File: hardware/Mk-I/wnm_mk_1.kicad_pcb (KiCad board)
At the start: 2 copper layers, 96.5 x 67.1 mm, 126 parts, among them CON1 USB-MICRO-B, SW1 SW_PUSH, SW10 SW_PUSH, SW11 SW_PUSH, SW12 SW_PUSH, SW13 SW_PUSH, SW14 SW_PUSH, SW15 SW_PUSH, SW16 SW_PUSH, SW18 SW_PUSH, SW19 SW_PUSH, SW2 SW_PUSH, SW20 SW_PUSH, SW21 SW_PUSH, SW22 SW_PUSH, SW3 SW_PUSH, SW4 SW_PUSH, SW5 SW_PUSH, SW6 SW_PUSH, SW7 SW_PUSH, SW8 SW_PUSH, SW9 SW_PUSH, U1 AP7313-18-SR-G-7, U10 STM32_SWD_Connector, U2 MCP73831, U3 BD33IA5, U4 STM32F407VG, U5 SGTL5000, U6 encoder_and_switch, U7 encoder_and_switch, U8 MOLEX_microSD_47219-2001, U9 SSD1306, X1 CRYSTAL

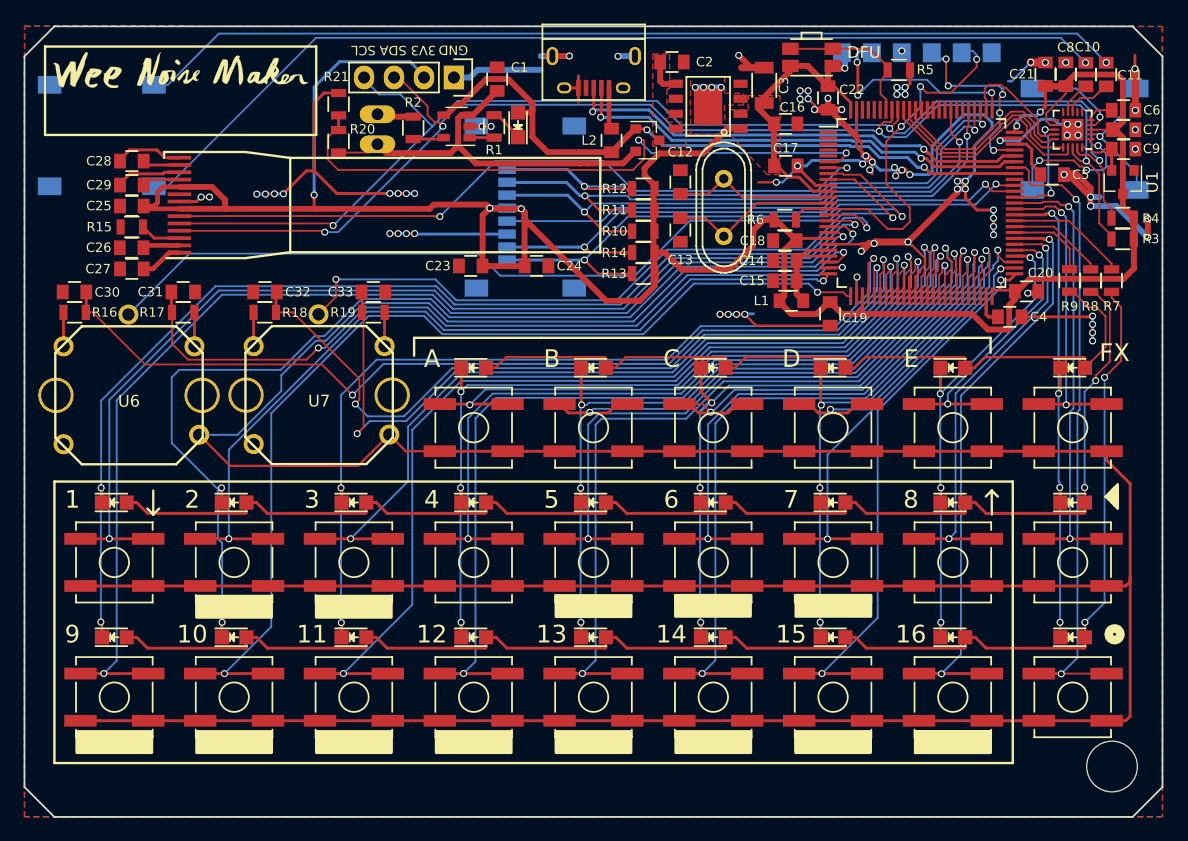
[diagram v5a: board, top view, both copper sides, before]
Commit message: HW: A couple of improvements in layout and ground
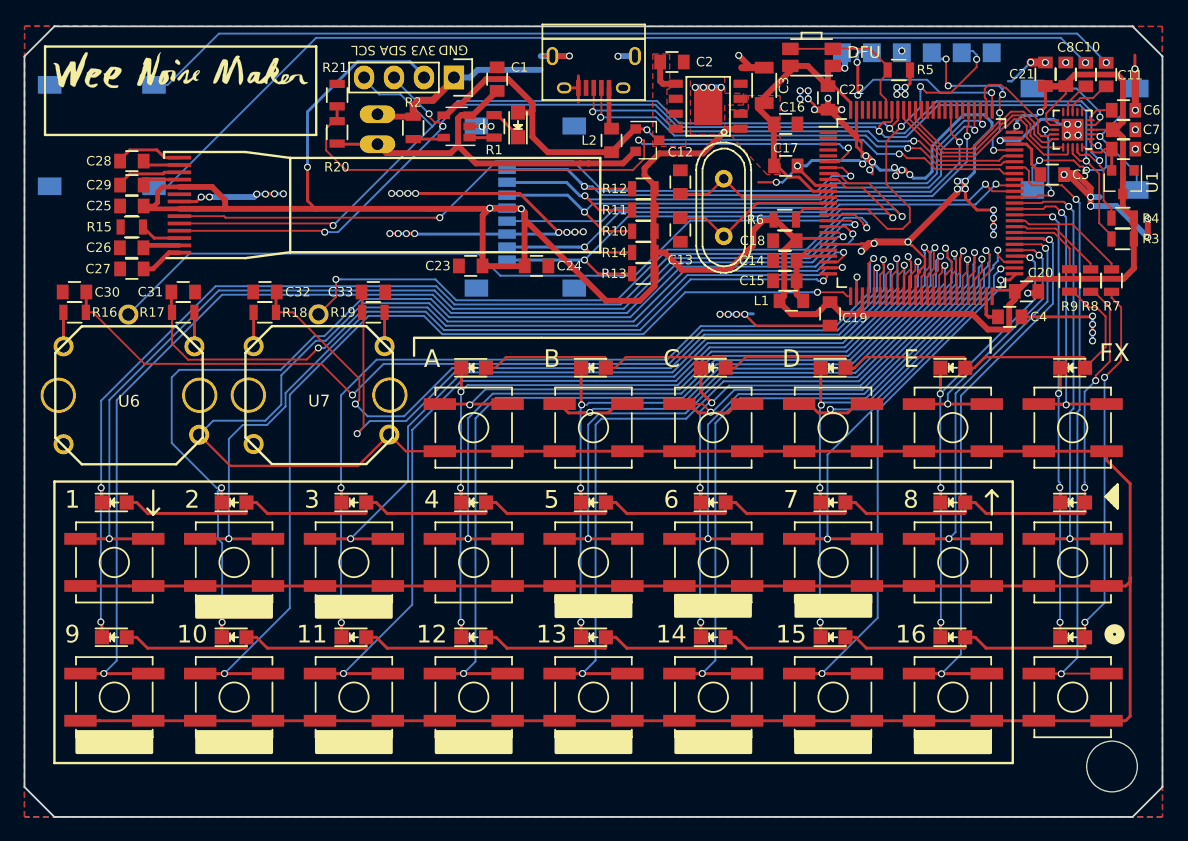
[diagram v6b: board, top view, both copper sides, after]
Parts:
- moved R21 0.78 mm to (106.5, 83.6)
- moved R20 0.77 mm to (106.5, 86.7)
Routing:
- net GND: track 211.1 -> 222.1 mm, vias 84 -> 88
- net B2: track 74.3 -> 75.5 mm
- net VBAT: track 33.9 -> 34.8 mm
- net Screen_NReset: track 62.0 -> 62.7 mm
- net WAKEUP: track 347.6 -> 348.3 mm
- net 3V3: track 245.3 -> 244.6 mm
- net B10: track 87.0 -> 86.3 mm
- net VBAT_SENSE: track 54.3 -> 54.8 mm
- net Audio_SDA: track 107.2 -> 107.0 mm, vias 4 -> 5

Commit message: HW: Enlarge screen footprint
To give room for more models.
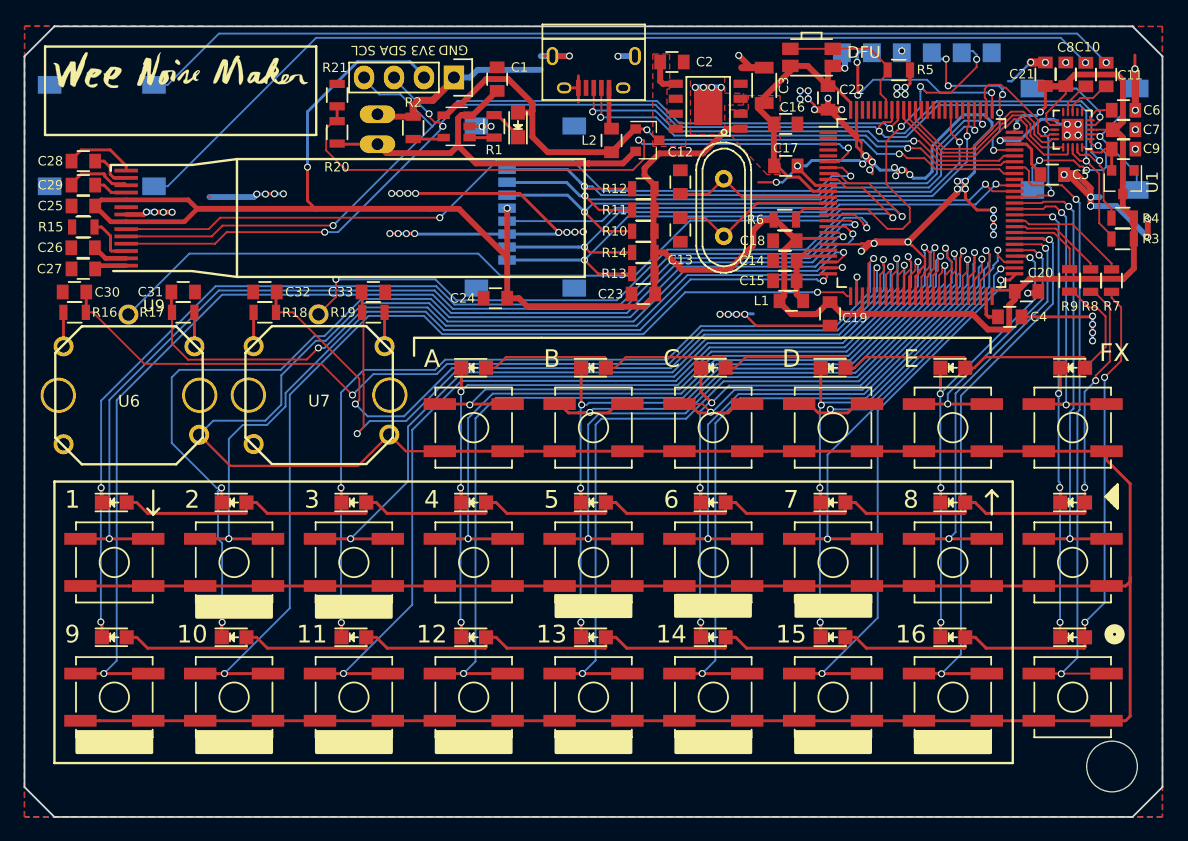
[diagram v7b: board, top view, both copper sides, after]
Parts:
- moved C23 14.8 mm to (132.5, 100.4)
- moved U9 4.65 mm to (87.4, 98.4)
- moved C24 4.44 mm to (120.0, 100.8), turned to 180 degrees
- moved C25 4.11 mm to (85.0, 93.0)
- moved C27 4.11 mm to (85.0, 98.3)
- moved C28 4.11 mm to (85.0, 89.2)
- moved C29 4.11 mm to (85.0, 91.2)
- moved R15 4.11 mm to (85.0, 94.7)
- moved C26 4.11 mm to (85.0, 96.5)
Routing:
- net Audio_SDA: track 107.0 -> 111.9 mm
- net Screen_NReset: track 62.7 -> 67.6 mm
- net Audio_SCL: track 107.2 -> 112.1 mm
- net 3V3: track 244.6 -> 240.4 mm, vias 6 -> 5
- net GND: track 222.1 -> 223.4 mm, vias 88 -> 90
- net Net-(C28-Pad2): track 3.17 -> 4.03 mm
- net Net-(C27-Pad1): track 3.60 -> 2.75 mm
- net Net-(R15-Pad1): track 3.47 -> 4.23 mm
- net Net-(C28-Pad1): track 6.61 -> 6.07 mm

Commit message: HW: Mk-I rev-C
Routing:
- net (no net): track 0.00 -> 6.39 mm, vias 0 -> 4
- net GND: track 223.4 -> 217.0 mm, vias 90 -> 86
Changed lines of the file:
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@@
-(kicad_pcb (version 4) (host pcbnew 4.0.5-e0-6337~52~ubuntu16.10.1)
+(kicad_pcb (version 4) (host pcbnew 4.0.6-e0-6349~52~ubuntu16.10.1)
   (general
     (links 345)
     (no_connects 0)
-    (area 79.933819 77.646179 176.605001 144.855001)
+    (area 66.563202 67.150001 181.907143 146.975)
     (thickness 1.6)
     (drawings 88)
@@
   )
   (setup
-    (last_trace_width 0.5)
+    (last_trace_width 0.25)
     (user_trace_width 0.16)
     (user_trace_width 0.2)
@@
       (drillshape 0)
       (scaleselection 1)
-      (outputdirectory Rev_B/gerber/))
+      (outputdirectory Rev_C/gerber/))
   )
   (net 0 "")
@@
     (effects (font (size 1.5 1.5) (thickness 0.3)))
   )
+  (segment (start 95.7 92.2) (end 99.4644 92.2) (width 0.5) (layer B.Cu) (net 0))
+  (segment (start 99.4644 92.2) (end 99.7116 91.9528) (width 0.5) (layer B.Cu) (net 0))
+  (segment (start 100.4482 91.9528) (end 99.7116 91.9528) (width 0.25) (layer B.Cu) (net 0))
+  (via (at 99.7116 91.9528) (size 0.6) (drill 0.4) (layers F.Cu B.Cu) (net 0))
+  (segment (start 101.2102 91.9274) (end 100.4736 91.9274) (width 0.25) (layer F.Cu) (net 0))
+  (segment (start 100.4736 91.9274) (end 100.4482 91.9528) (width 0.25) (layer F.Cu) (net 0))
+  (via (at 100.4482 91.9528) (size 0.6) (drill 0.4) (layers F.Cu B.Cu) (net 0))
+  (segment (start 101.9722 91.9274) (end 101.2102 91.9274) (width 0.25) (layer B.Cu) (net 0))
+  (via (at 101.2102 91.9274) (size 0.6) (drill 0.4) (layers F.Cu B.Cu) (net 0))
+  (via (at 101.9722 91.9274) (size 0.6) (drill 0.4) (layers F.Cu B.Cu) (net 0))
+  (segment (start 95.698 92.202) (end 95.7 92.2) (width 0.25) (layer F.Cu) (net 0))
   (segment (start 130.561477 101.315123) (end 134.854074 97.022526) (width 0.16) (layer B.Cu) (net 1))
   (segment (start 134.854074 97.022526) (end 146.470931 97.022525) (width 0.16) (layer B.Cu) (net 1))
@@
   (segment (start 125.1792 95.3436) (end 125.3236 95.1992) (width 0.25) (layer B.Cu) (net 31))
   (via (at 125.3236 95.1992) (size 0.6) (drill 0.4) (layers F.Cu B.Cu) (net 31))
-  (segment (start 95.7 92.2) (end 99.4644 92.2) (width 0.5) (layer B.Cu) (net 31))
-  (segment (start 99.4644 92.2) (end 99.7116 91.9528) (width 0.5) (layer B.Cu) (net 31))
-  (segment (start 100.4482 91.9528) (end 99.7116 91.9528) (width 0.25) (layer B.Cu) (net 31))
-  (via (at 99.7116 91.9528) (size 0.6) (drill 0.4) (layers F.Cu B.Cu) (net 31))
-  (segment (start 101.2102 91.9274) (end 100.4736 91.9274) (width 0.25) (layer F.Cu) (net 31))
-  (segment (start 100.4736 91.9274) (end 100.4482 91.9528) (width 0.25) (layer F.Cu) (net 31))
-  (via (at 100.4482 91.9528) (size 0.6) (drill 0.4) (layers F.Cu B.Cu) (net 31))
-  (segment (start 101.9722 91.9274) (end 101.2102 91.9274) (width 0.25) (layer B.Cu) (net 31))
-  (via (at 101.2102 91.9274) (size 0.6) (drill 0.4) (layers F.Cu B.Cu) (net 31))
-  (via (at 101.9722 91.9274) (size 0.6) (drill 0.4) (layers F.Cu B.Cu) (net 31))
   (segment (start 154.4368 79.8116) (end 154.4232 79.8116) (width 0.5) (layer B.Cu) (net 31))
   (segment (start 154.4447 79.8195) (end 154.4368 79.8116) (width 0.5) (layer B.Cu) (net 31))
@@
   (via (at 113.1 95.3) (size 0.6) (drill 0.4) (layers F.Cu B.Cu) (net 31))
   (segment (start 113.1436 95.3436) (end 113.1 95.3) (width 0.25) (layer B.Cu) (net 31))
-  (segment (start 95.698 92.202) (end 95.7 92.2) (width 0.25) (layer F.Cu) (net 31))
   (segment (start 138.3 82.9) (end 139.1 82.9) (width 0.5) (layer B.Cu) (net 31))
   (via (at 139.1 82.9) (size 0.6) (drill 0.4) (layers F.Cu B.Cu) (net 31))
